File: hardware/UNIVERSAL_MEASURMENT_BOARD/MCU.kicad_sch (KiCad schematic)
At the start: 8 parts, among them U4 STM32G0C1KCT6N, U6 ADS8863IDGS, Y2 ECS-1612MV

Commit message: continued
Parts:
- removed C1, C2, C3: C, symbol Device:C
- added C1, C2: 100nF, symbol Device:C_Small
- added C3: 10nF, symbol Device:C_Small
- added C4: -F, symbol Device:C_Small
- renumbered C4 to C6, U6 to U1, U4 to U2, Y2 to Y1
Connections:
- net +3V3: now also C1.1; no longer U1.2 (AVDD)
- net GND: now also C1.2, C2.2, C3.2, C4.2
- net at U1.1 (REF): now also C4.1
- new net +3V3A: C2.1, C3.1, U1.2 (AVDD)
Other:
- company: (none) -> PUT Motorsport Formula Student team
- title: (none) -> Universal Measurment Board
- moved on the sheet: C5, C6, U1, U2, Y1

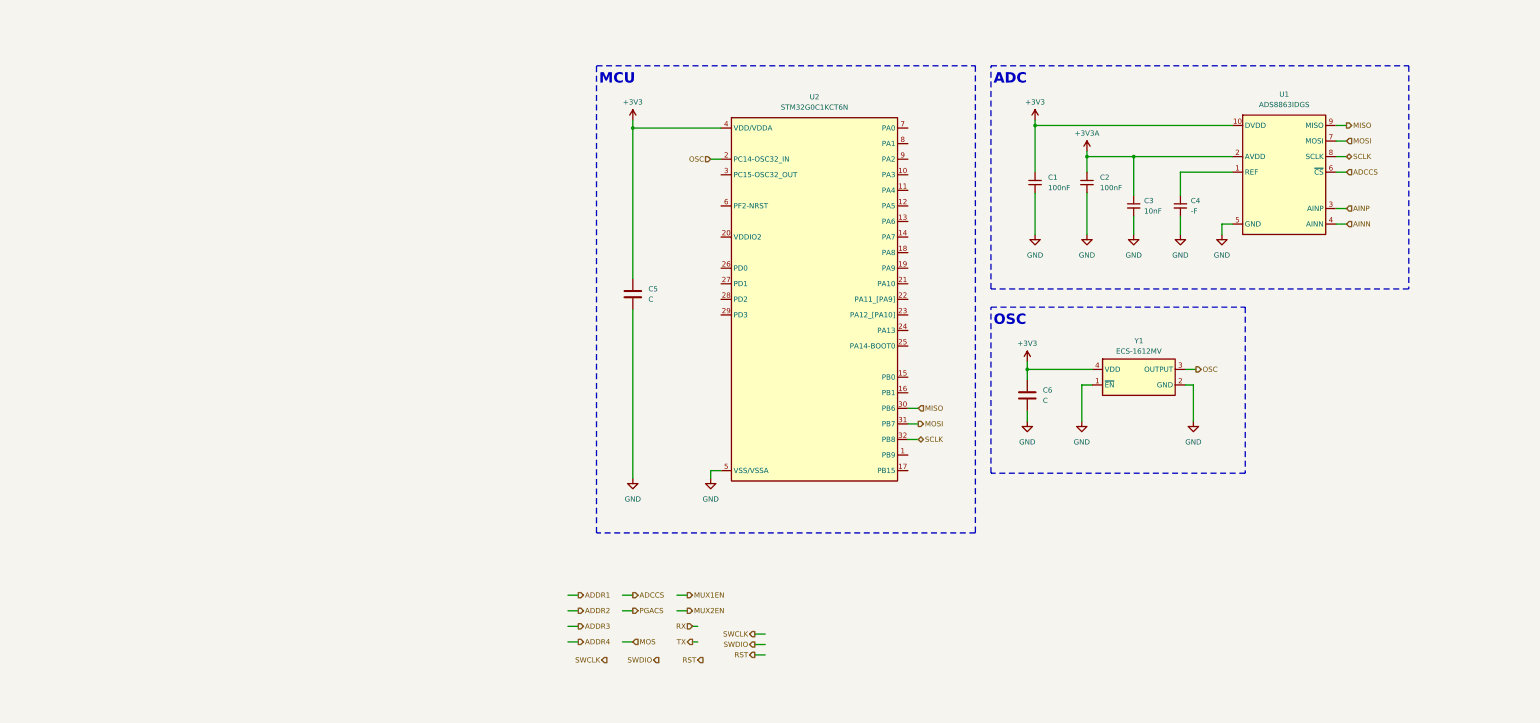
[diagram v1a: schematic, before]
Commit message: schematic review corrections
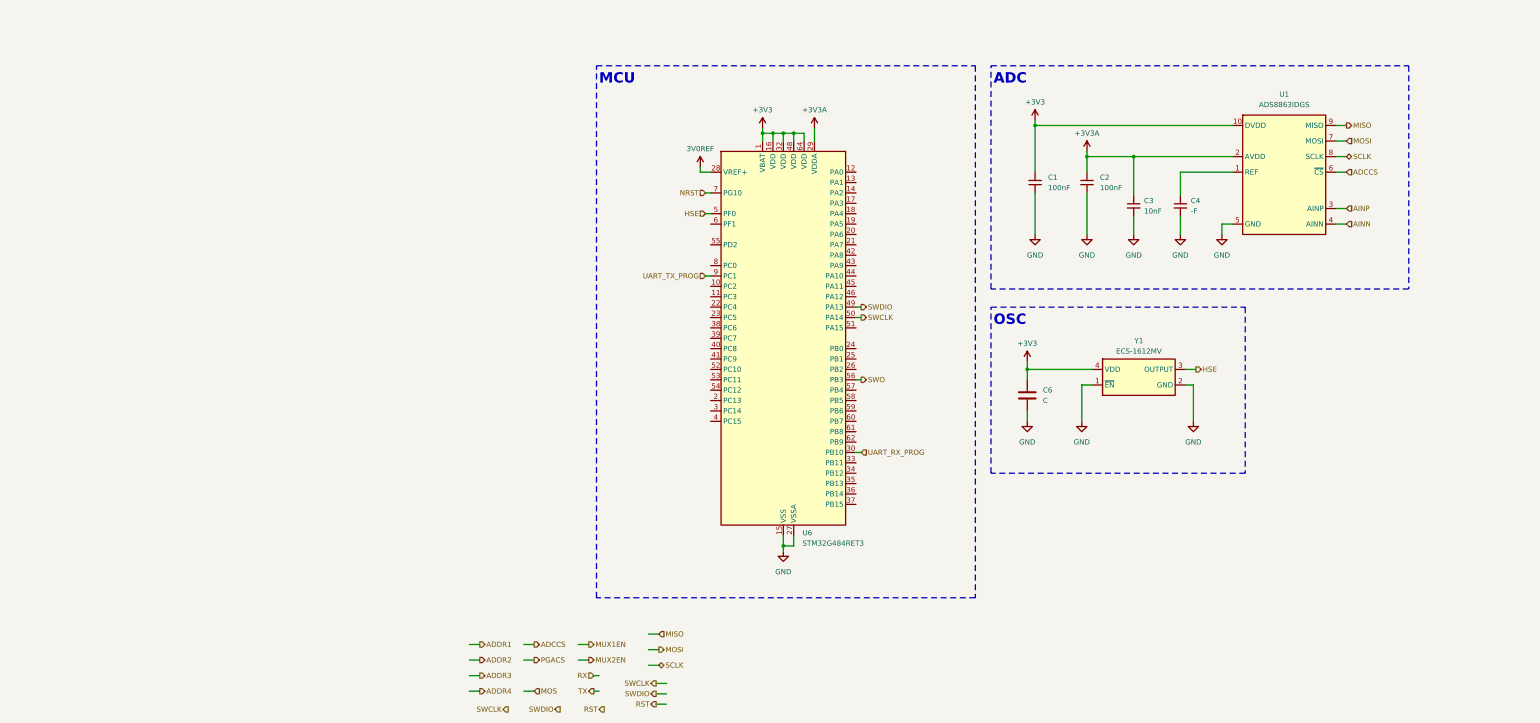
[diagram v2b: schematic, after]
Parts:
- removed C5: C, symbol Device:C
- removed U2: STM32G0C1KCT6N, QFP80P900X900X160-32N, symbol STM32G0C1KCT6N:STM32G0C1KCT6N
- added U6: STM32G484RET3, QFP50P1200X1200X160-64N, symbol STM32G484RET3:STM32G484RET3
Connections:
- net +3V3: now also U6.1 (VBAT), U6.16 (VDD), U6.32 (VDD), U6.48 (VDD), U6.64 (VDD)
- net +3V3A: now also U6.29 (VDDA)
- net GND: now also U6.15 (VSS), U6.27 (VSSA), U6.31 (VSS), U6.47 (VSS), U6.63 (VSS)
- net SWCLK: now also U6.50 (PA14)
- net SWDIO: now also U6.49 (PA13)
- net OSC renamed HSE
- net HSE: now also U6.5 (PF0)
- new net 3V0REF: U6.28 (VREF+)
- new net NRST: U6.7 (PG10)
- new net SWO: U6.56 (PB3)
- new net UART_RX_PROG: U6.30 (PB10)
- new net UART_TX_PROG: U6.9 (PC1)

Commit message: final schematic review corrections
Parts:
- removed C6: C, symbol Device:C
- added C42: 100nF, symbol Device:C_Small
- added C6: 10pF, symbol Device:C_Small
- C4: value -F -> 100nF
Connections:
- net +3V3: now also C42.1
- net GND: now also C42.2, C6.2
- net HSE: now also C6.1
- net +3V0A: now reaches C4.1, U1.1 (REF)
- net 3V0REF renamed 3V0A
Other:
- note added: "Analog to Digital Converter"
- note added: "HSE"
- note added: "MCU Clock"
- note added: "Microcontroller"
- note added: "To connect to mcu:"
- note removed: "OSC"
- moved on the sheet: C1, C2, C3, C4, U1, U6, Y1

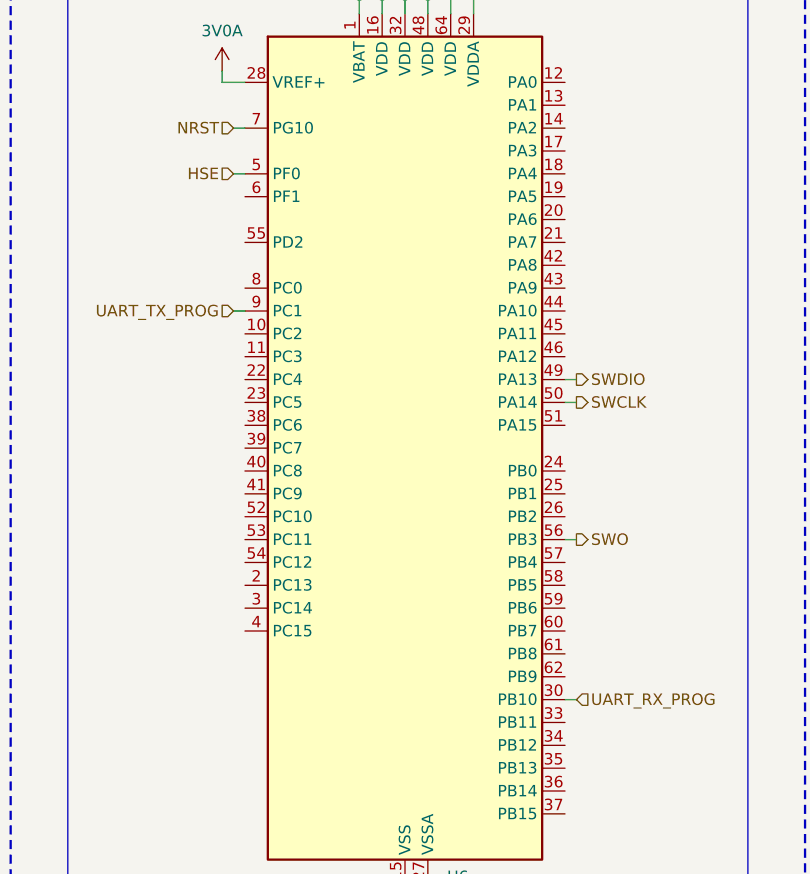
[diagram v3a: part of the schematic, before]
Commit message: added footprints
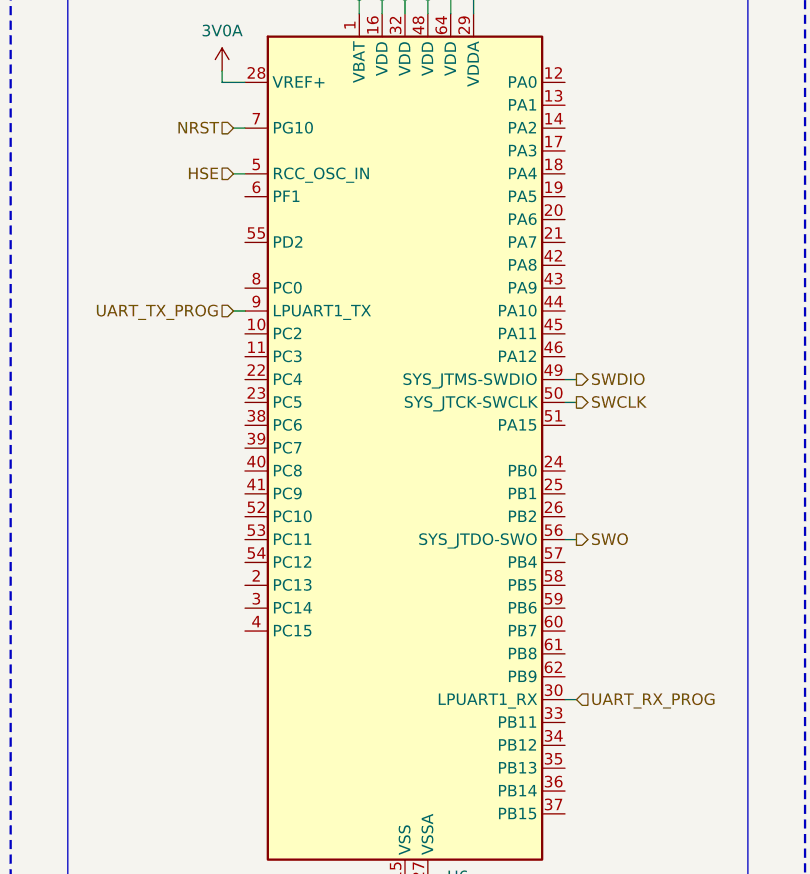
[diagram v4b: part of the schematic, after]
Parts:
- C1, C2, C3, C4, C42, C6: footprint (none) -> Capacitor_SMD:C_0603_1608Metric
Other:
- company: PUT Motorsport Formula Student team -> PUT Motorsport Formula Student Team
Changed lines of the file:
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@@
 		(title "Universal Measurment Board")
 		(date "2026-02-02")
-		(rev "1.7.14")
-		(company "PUT Motorsport Formula Student team")
+		(rev "1.7.15")
+		(company "PUT Motorsport Formula Student Team")
 		(comment 1 "Designed by Marcin Trzmiel under")
 	)
@@
 		)
 		(pin "56"
+			(alternate "SYS_JTDO-SWO")
 		)
 		(pin "33"
@@
 		)
 		(pin "30"
+			(alternate "LPUART1_RX")
 		)
 		(pin "44"
 		)
 		(pin "49"
+			(alternate "SYS_JTMS-SWDIO")
 		)
 		(pin "64"
@@
 		)
 		(pin "50"
+			(alternate "SYS_JTCK-SWCLK")
 		)
 		(pin "51"
@@
 		)
 		(pin "5"
+			(alternate "RCC_OSC_IN")
 		)
 		(pin "7"
@@
 		)
 		(pin "9"
+			(alternate "LPUART1_TX")
 		)
 		(pin "39"
@@
 			)
 		)
-		(property "Footprint" ""
+		(property "Footprint" "Capacitor_SMD:C_0603_1608Metric"
 			(at 158.75 116.84 0)
 			(effects
@@
 			)
 		)
-		(property "Footprint" ""
+		(property "Footprint" "Capacitor_SMD:C_0603_1608Metric"
 			(at 207.645 116.84 0)
 			(effects
@@
 			)
 		)
-		(property "Footprint" ""
+		(property "Footprint" "Capacitor_SMD:C_0603_1608Metric"
 			(at 158.75 62.23 0)
 			(effects
@@
 			)
 		)
-		(property "Footprint" ""
+		(property "Footprint" "Capacitor_SMD:C_0603_1608Metric"
 			(at 171.45 66.04 0)
 			(effects
@@
 			)
 		)
-		(property "Footprint" ""
+		(property "Footprint" "Capacitor_SMD:C_0603_1608Metric"
 			(at 184.785 66.04 0)
 			(effects
@@
 			)
 		)
-		(property "Footprint" ""
+		(property "Footprint" "Capacitor_SMD:C_0603_1608Metric"
 			(at 196.215 69.215 0)
 			(effects

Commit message: first outcom of pcb design
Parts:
- added C75, C76, C77, C78, C79: 100nF, REST:C_0603_1608Metric, symbol Device:C_Small
- C1, C6: footprint Capacitor_SMD:C_0603_1608Metric -> REST:C_0603_1608Metric
- C2: renamed from C42; footprint Capacitor_SMD:C_0603_1608Metric -> REST:C_0603_1608Metric
- C3: renamed from C2; footprint Capacitor_SMD:C_0603_1608Metric -> REST:C_0603_1608Metric
- C4: renamed from C3; footprint Capacitor_SMD:C_0603_1608Metric -> REST:C_0603_1608Metric
- C5: renamed from C4; footprint Capacitor_SMD:C_0603_1608Metric -> REST:C_0603_1608Metric
- renumbered U6 to U1, U1 to U2
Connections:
- net +3V3: now also C75.1, C76.1, C77.1, C78.1
- net +3V3A: now also C79.1
- net ADCCS: now also U1.22 (PC4)
- net ADDR1: now also U1.12 (PA0)
- net ADDR2: now also U1.11 (PC3)
- net ADDR3: now also U1.14 (PA2)
- net CAN_RX: now also U1.53 (PC11)
- net CAN_STB: now also U1.51 (PA15)
- net CAN_TX: now also U1.52 (PC10)
- net GND: now also C75.2, C76.2, C77.2, C78.2, C79.2
- net MISO: now also U1.20 (PA6)
- net MOSI: now also U1.21 (PA7)
- net MUXEN: now also U1.13 (PA1)
- net PGACS: now also U1.17 (PA3)
- net SCLK: now also U1.19 (PA5)

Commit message: Review fixes
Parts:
- removed Y1: ECS-1612MV, ECS1612MV080CNTR, symbol ECS-1612MV-080-CN-TR:ECS-1612MV-080-CN-TR
- added Y1: ATX-H11-F-16.000MHz-G100-T, ATXH11F16000MHzG100T, symbol ATX-H11-F-16.000MHz-G100-T:ATX-H11-F-16.000MHz-G100-T
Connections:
- net +3V3: now also Y1.1 (~{INH}), Y1.4 (VDD)
- net ADCCS: now also U1.18 (PA4); no longer U1.22 (PC4)
- net ADDR1: now also U1.33 (PB11); no longer U1.12 (PA0)
- net ADDR2: now also U1.34 (PB12); no longer U1.11 (PC3)
- net ADDR3: now also U1.36 (PB14); no longer U1.14 (PA2)
- net GND: now also Y1.2 (GND)
- net HSE: now also Y1.3 (OUTPUT)
- net MUXEN: now also U1.35 (PB13); no longer U1.13 (PA1)

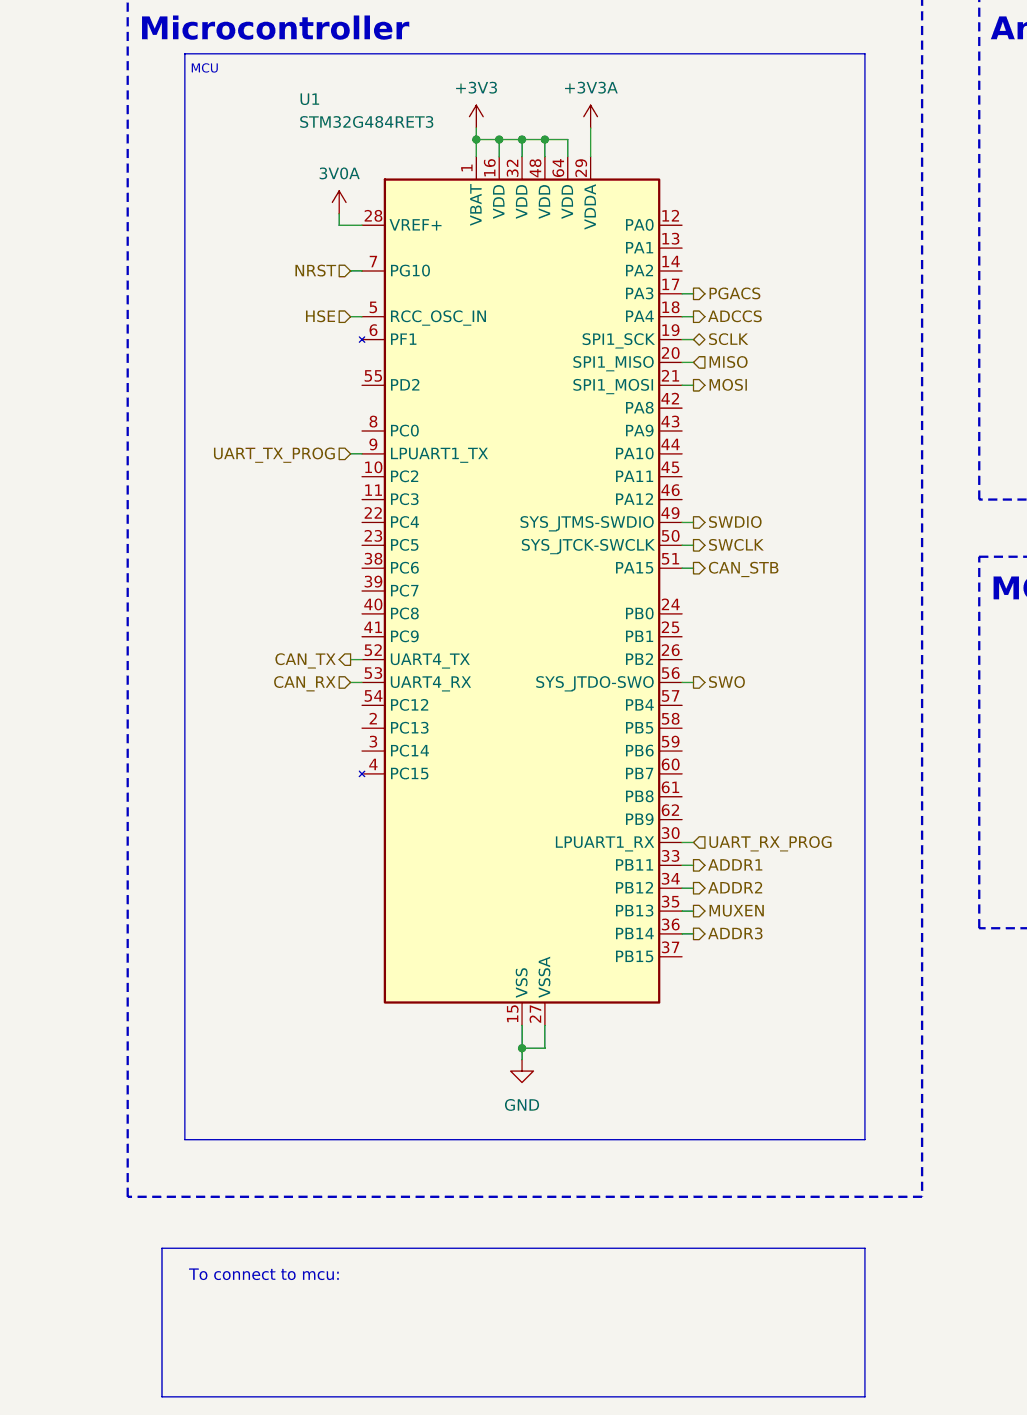
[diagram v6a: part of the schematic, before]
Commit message: solved DRC problems
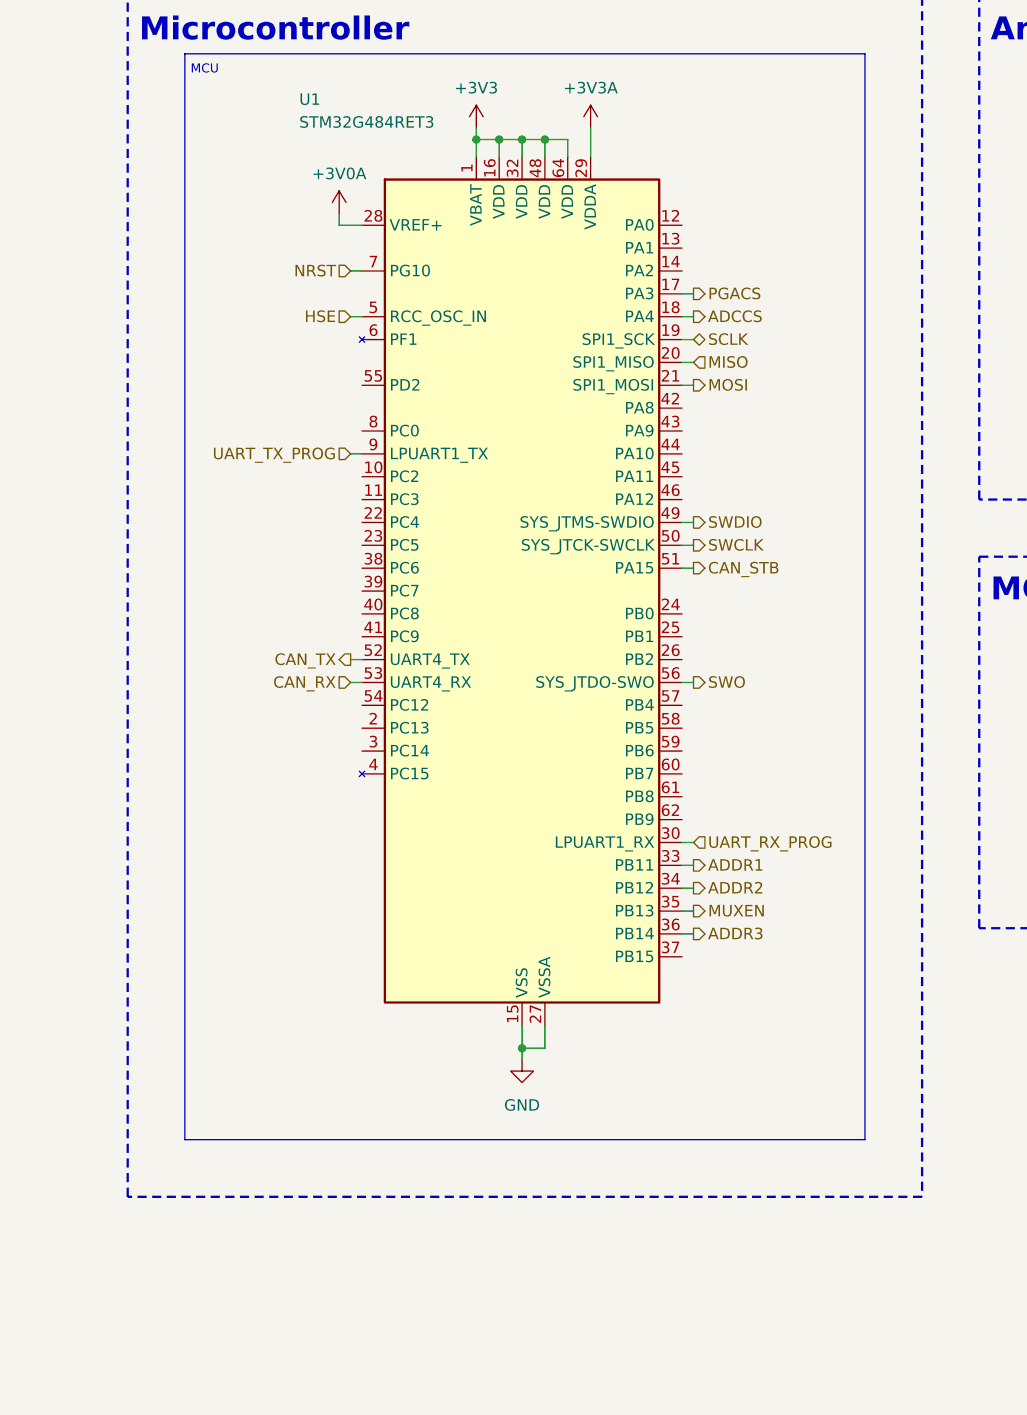
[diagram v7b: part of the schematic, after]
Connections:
- net 3V0A is gone; now on net +3V0A: U1.28 (VREF+)
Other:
- note removed: "To connect to mcu:"
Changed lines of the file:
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@@
 	(title_block
 		(title "Universal Measurment Board")
-		(date "2026-02-02")
-		(rev "1.7.15")
+		(date "2026-03-26")
+		(rev "1.9.21")
 		(company "PUT Motorsport Formula Student Team")
 		(comment 1 "Designed by Marcin Trzmiel under")
@@
 		(start 58.42 38.735)
 		(end 133.985 159.385)
-		(stroke
-			(width 0)
-			(type solid)
-			(color 200 200 200 1)
-		)
-		(fill
-			(type none)
-		)
-	)
-	(rectangle
-		(start 55.88 171.45)
-		(end 133.985 187.96)
 		(stroke
 			(width 0)
@@
 			)
 			(justify left top)
-		)
-	)
-	(text "To connect to mcu:"
-		(exclude_from_sim no)
-		(at 67.31 174.625 0)
-		(effects
-			(font
-				(size 1.27 1.27)
-				(color 0 0 0 0.53)
-			)
 		)
 	)
@@
 			)
 		)
-		(property "Value" "3V0A"
+		(property "Value" "+3V0A"
 			(at 75.565 52.07 0)
 			(show_name no)
